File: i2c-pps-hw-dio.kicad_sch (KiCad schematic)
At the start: 19 parts, among them J3 Digital I/O, U2 AP2210-3.3, U3 74AHC1G14

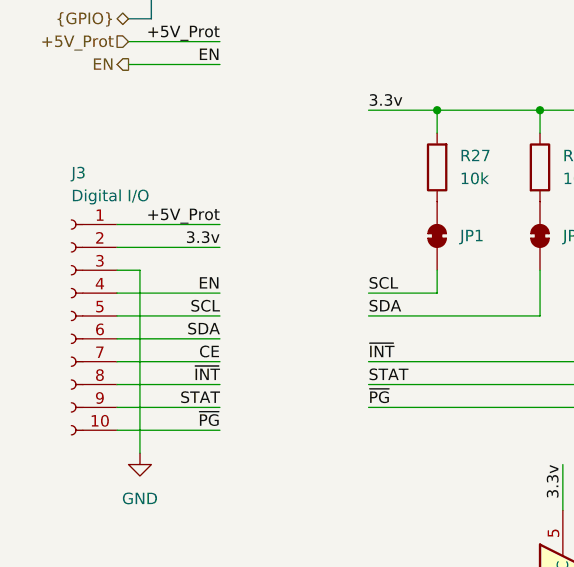
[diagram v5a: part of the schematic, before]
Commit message: Implement approximate component placement
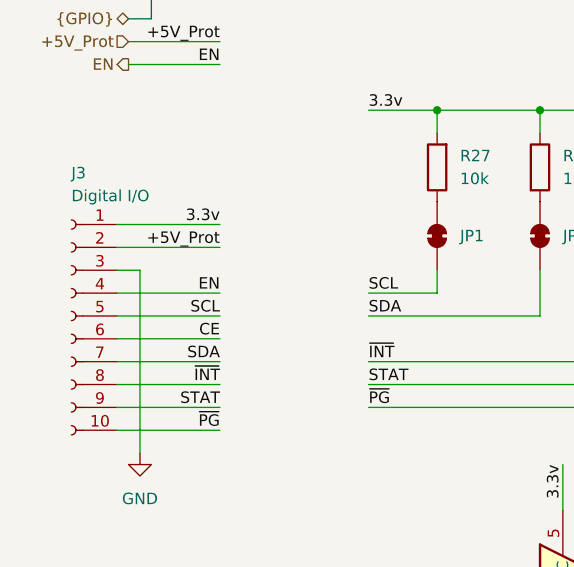
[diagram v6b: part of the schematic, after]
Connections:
- net +5V_Prot: now also J3.2 (Pin_2); no longer J3.1 (Pin_1)
- net 3.3v: now also J3.1 (Pin_1); no longer J3.2 (Pin_2)
- net CE: now also J3.6 (Pin_6); no longer J3.7 (Pin_7)
- net SDA: now also J3.7 (Pin_7); no longer J3.6 (Pin_6)

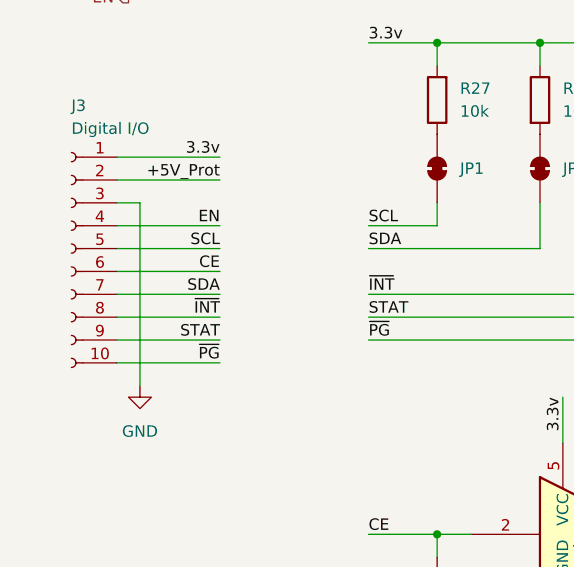
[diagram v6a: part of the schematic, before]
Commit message: Route the PCB
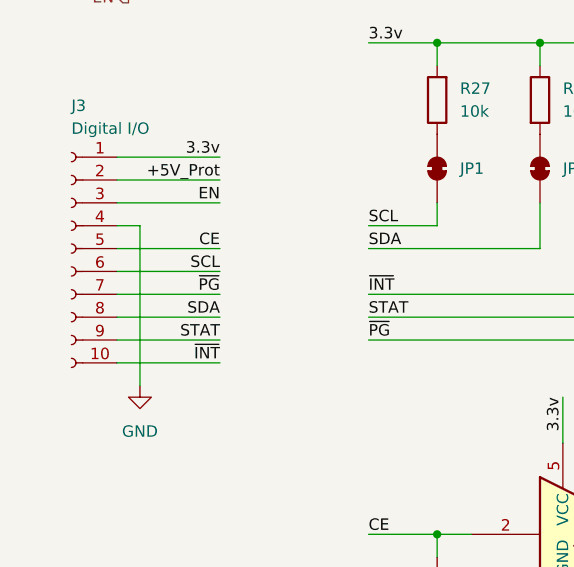
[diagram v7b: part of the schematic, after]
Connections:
- net CE: now also J3.5 (Pin_5); no longer J3.6 (Pin_6)
- net EN: now also J3.3 (Pin_3); no longer J3.4 (Pin_4)
- net GND: now also J3.4 (Pin_4); no longer J3.3 (Pin_3)
- net SCL: now also J3.6 (Pin_6); no longer J3.5 (Pin_5)
- net SDA: now also J3.8 (Pin_8); no longer J3.7 (Pin_7)
- net ~{INT}: now also J3.10 (Pin_10); no longer J3.8 (Pin_8)
- net ~{PG}: now also J3.7 (Pin_7); no longer J3.10 (Pin_10)
